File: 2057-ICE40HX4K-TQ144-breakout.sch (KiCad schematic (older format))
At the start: 73 parts, among them J1 Conn_02x30_Odd_Even, J2 Conn_02x30_Odd_Even, J3 RaspberryPI-B+header, J4 0548190519, J5 RaspberryPI-B+header, J6 Conn_02x08_Odd_Even, J7 Conn_02x01, J8 Micro_SD_Card_Det, U1 ICE40HX4K-TQ144, U2 AZ1117CH-3.3TRG1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

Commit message: Change USB connector, re-route SD & buttons
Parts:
- removed J4: 0548190519, digikey-footprints:USB_Mini_B_Female_548190519, symbol dk_USB-DVI-HDMI-Connectors:0548190519
- added J4: USB4105-GF-A, jb-footprint:USB_C_Receptacle_HRO_TYPE-C-31-M-12, symbol JWlib:USB4105-GF-A
- added R17, R18: 5.1K, Resistor_SMD:R_0603_1608Metric_Pad1.05x0.95mm_HandSolder, symbol Device:R
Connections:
- net +5V: now also J4.A4, J4.A9, J4.B4, J4.B9
- net GND: now also J8.9 (DET_B), J4.A1, J4.A12, J4.B1, J4.B12, J4.S1, R17.1, R18.2; no longer J8.10 (DET_A)
- net IOR_161: now also S1.1
- net IOR_165: now also S2.1
- net IOT_174: now also J8.2 (DAT3/CD)
- net IOT_178: now also J8.3 (CMD)
- net IOT_181: now also J8.7 (DAT0)
- net IOT_191: now also J8.5 (CLK)
- net IOT_192: now also J8.10 (DET_A)
- net IOT_206: no longer J8.2 (DAT3/CD)
- net IOT_213: no longer J8.3 (CMD)
- net IOT_215: no longer J8.5 (CLK)
- net IOT_217: no longer J8.7 (DAT0)
- net IOT_219: no longer S2.1
- net IOT_220: no longer J8.9 (DET_B), S1.1
- new net: J4.A5, R17.2
- new net: J4.B5, R18.1
- no-connect marks 9 -> 12
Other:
- moved on the sheet: D2, R6, TP1, TP2, Y1

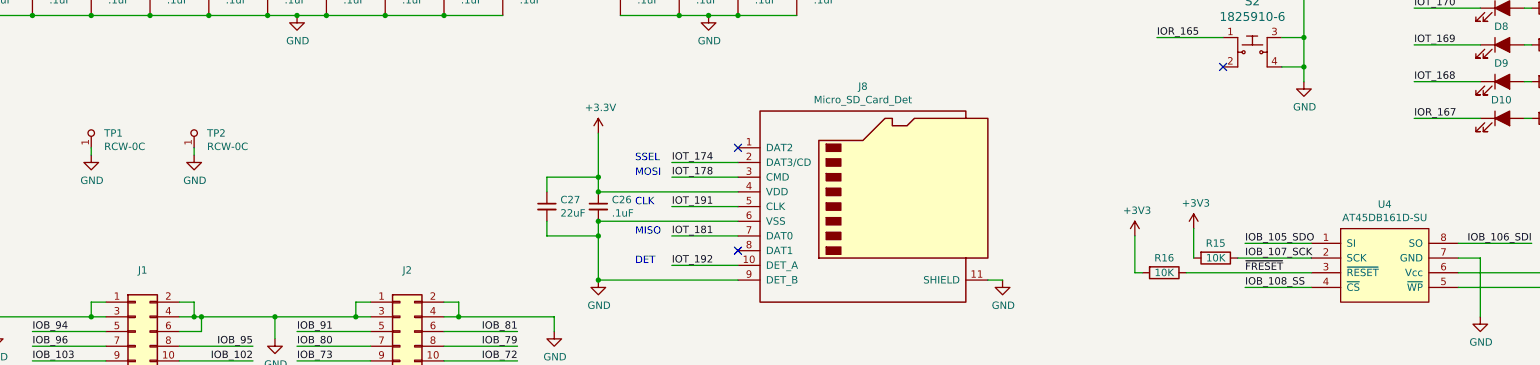
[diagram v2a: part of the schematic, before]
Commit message: Update BOM.
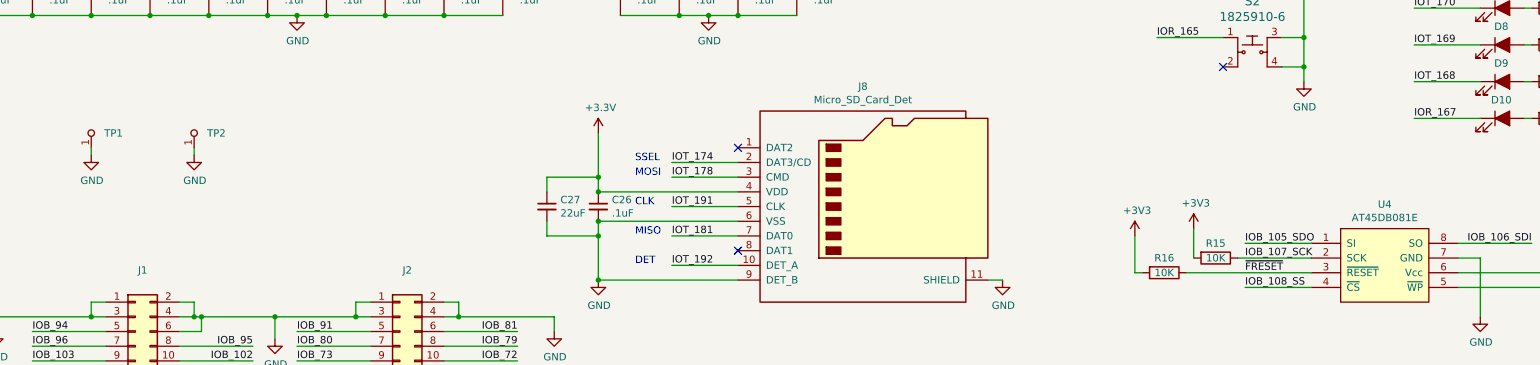
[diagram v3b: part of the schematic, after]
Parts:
- C1, C10, C11, C12, C13, C14, C15, C16, C17, C2, C22, C23, C24, C4, C6, C7, C8, C9: Description (none) -> CAP CER 0.1UF 50V X7R 0603; Manufacturer TDK -> TDK Corporation
- C18, C20, C3, C5: Description (none) -> CAP CER 10UF 6.3V X5R 0603; Manufacturer (none) -> Samsung Electro-Mechanics
- C19, C21, C27: Description (none) -> CAP CER 22UF 6.3V X5R 0603; Manufacturer (none) -> Samsung Electro-Mechanics
- C25: Description (none) -> CAP CER 4.7UF 6.3V X5R 0603; Digi-Key_PN (none) -> 1276-1045-1-ND; MPN (none) -> CL10A475KQ8NNNC; Manufacturer (none) -> Samsung Electro-Mechanics
- C26: Description (none) -> CAP CER 0.1UF 50V X7R 0603; Digi-Key_PN (none) -> 445-1314-1-ND; MPN (none) -> C1608X7R1H104K080AA; Manufacturer (none) -> TDK Corporation
- D1, D11, D12: Description (none) -> DIODE GEN PURP 75V 250MA SOD323F
- J1, J2: Description (none) -> Connector Header Through Hole 60 position 0.100\" (2.54mm); Digi-Key_PN (none) -> S2011EC-30-ND; MPN (none) -> PRPC030DAAN-RC; Manufacturer (none) -> Sullins Connector Solutions
- J3, J5: Description (none) -> Connector Header Through Hole 40 position 0.100\" (2.54mm); Digi-Key_PN (none) -> S2011EC-20-ND; MPN (none) -> PRPC020DAAN-RC; Manufacturer (none) -> Sullins Connector Solutions
- J6: Description (none) -> Connector Header Through Hole 16 position 0.100\" (2.54mm); Digi-Key_PN (none) -> 10129381-916001BLF-ND; MPN (none) -> 10129381-916001BLF; Manufacturer (none) -> Amphenol ICC (FCI)
- J7: Description (none) -> Connector Header Through Hole 2 position 0.100\" (2.54mm); Digi-Key_PN (none) -> 2057-PH1-02-UA-ND; MPN (none) -> PH1-02-UA; Manufacturer (none) -> Adam Tech
- J8: Description (none) -> 10 (8 + 2) Position Card Connector Secure Digital - microSD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; Digi-Key_PN (none) -> HR1941CT-ND; MPN (none) -> DM3D-SF; Manufacturer (none) -> Hirose Electric Co Ltd
- R1, R2: Description (none) -> RES 100 OHM 1% 1/10W 0603; Digi-Key_PN (none) -> 311-100HRCT-ND; MPN (none) -> RC0603FR-07100RL; Manufacturer (none) -> YAGEO
- R10, R11, R12, R13, R14, R6, R7, R8, R9: Description (none) -> RES 330 OHM 1% 1/10W 0603; Digi-Key_PN (none) -> 311-330HRCT-ND; MPN (none) -> RC0603FR-07330RL; Manufacturer (none) -> YAGEO
- R15, R16, R3, R4, R5: Description (none) -> RES 10K OHM 1% 1/10W 0603; Digi-Key_PN (none) -> 311-10.0KHRCT-ND; MPN (none) -> RC0603FR-0710KL; Manufacturer (none) -> YAGEO
- R17, R18: Description (none) -> RES SMD 5.1K OHM 1% 1/10W 0603; Digi-Key_PN (none) -> CR0603-FX-5101ELFCT-ND; MPN (none) -> CR0603-FX-5101ELF; Manufacturer (none) -> Bourns Inc.
- TP1: value RCW-0C -> RCWCTE; Description PC TEST POINT NATURAL -> PC TEST POINT; Digi-Key_PN A106146CT-ND -> 2019-RCWCTECT-ND; MPN RCW-0C -> RCWCTE; Manufacturer TE Connectivity AMP Connectors -> KOA Speer Electronics, Inc.
- TP2: value RCW-0C -> RCWCTE; Category Test and Measurement -> (none); DK_Datasheet_Link https://www.te.com/commerce/DocumentDelivery/DDEController?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 -> (none); DK_Detail_Page /product-detail/en/te-connectivity-amp-connectors/RCW-0C/A1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 -> https://www.digikey.com/short/32595572; Description PC TEST POINT NATURAL -> PC TEST POINT; Digi-Key_PN A106146CT-ND -> 2019-RCWCTECT-ND; Family Test Points -> (none); MPN RCW-0C -> RCWCTE; Manufacturer TE Connectivity AMP Connectors -> KOA Speer Electronics, Inc.; Status Active -> (none)
- U1: Description (none) -> IC FPGA 107 I/O 144TQFP; Manufacturer (none) -> Lattice Semiconductor Corporation
- U2: Description (none) -> IC REG LINEAR 3.3V 1A SOT223; Manufacturer (none) -> Diodes Incorporated
- U3: Description (none) -> IC REG LINEAR 1.2V 1A SOT223; Manufacturer (none) -> Diodes Incorporated
- U4: value AT45DB161D-SU -> AT45DB081E; Description (none) -> FLASH Memory IC 8Mbit SPI 85 MHz 8-SOIC; Digi-Key_PN (none) -> 1265-1092-1-ND; MPN (none) -> AT45DB081E-SSHNHC-T; Manufacturer (none) -> Renesas Design Germany GmbH

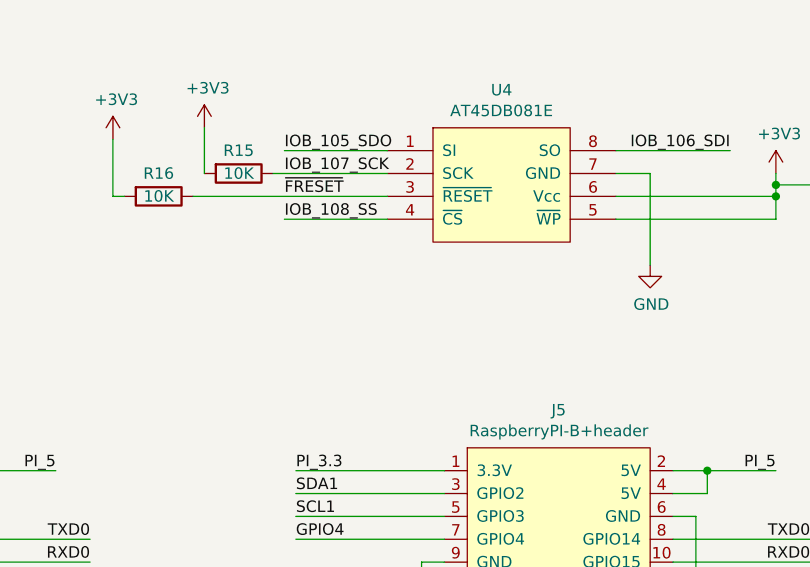
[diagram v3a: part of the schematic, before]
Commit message: Add notes of alternate FLASH chips
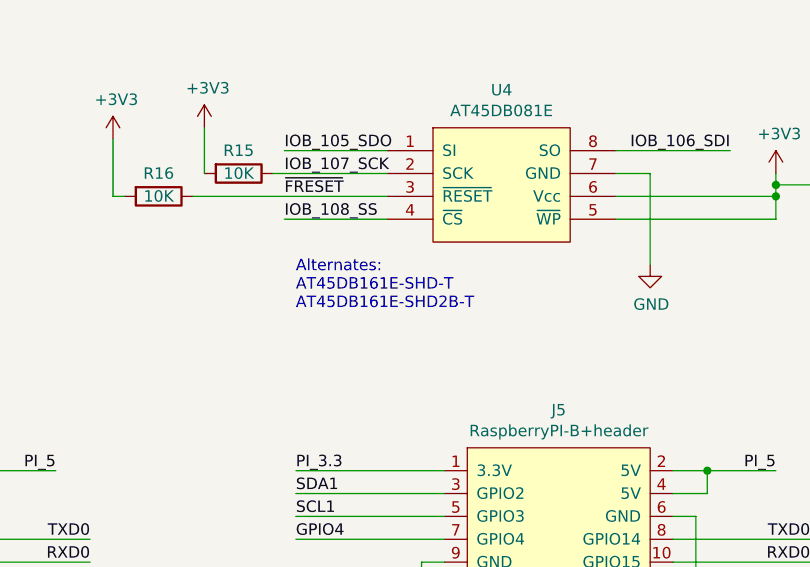
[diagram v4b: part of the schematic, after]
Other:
- note added: "Alternates: \nAT45DB161E-SHD-T\nAT45DB161E-SHD2B-T"
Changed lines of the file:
@@
 	1    0    0    -1
 $EndComp
+Text Notes 9700 7400 0    50   ~ 0
+Alternates:  \nAT45DB161E-SHD-T\nAT45DB161E-SHD2B-T
 $EndSCHEMATC
